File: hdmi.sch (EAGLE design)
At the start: 156 parts, among them IC1 FT2232HL, U0 6SLX45CSG324, U1 MT41J64M16, U2 TPD12S016RKTR, U3 TPD12S016RKTR, U4 TPD12S016RKTR, U5 MNR18, U6 MNR18, U8 20Mhz

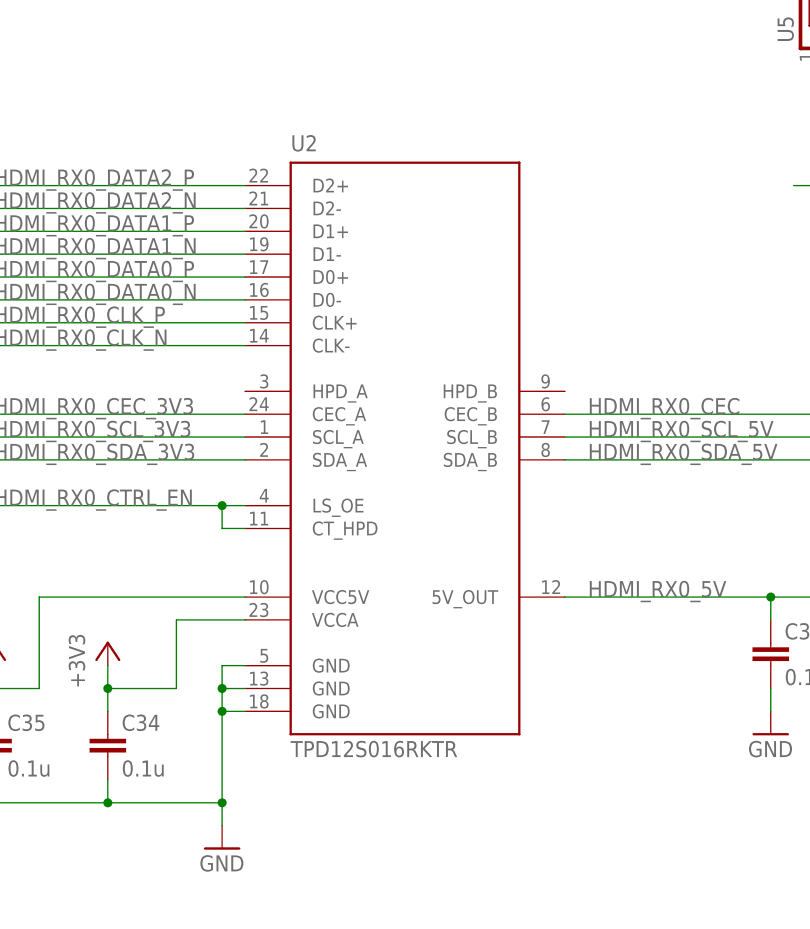
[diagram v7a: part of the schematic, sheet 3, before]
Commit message: Switched HDMI companion chip package, finished routing of the first HDMI group
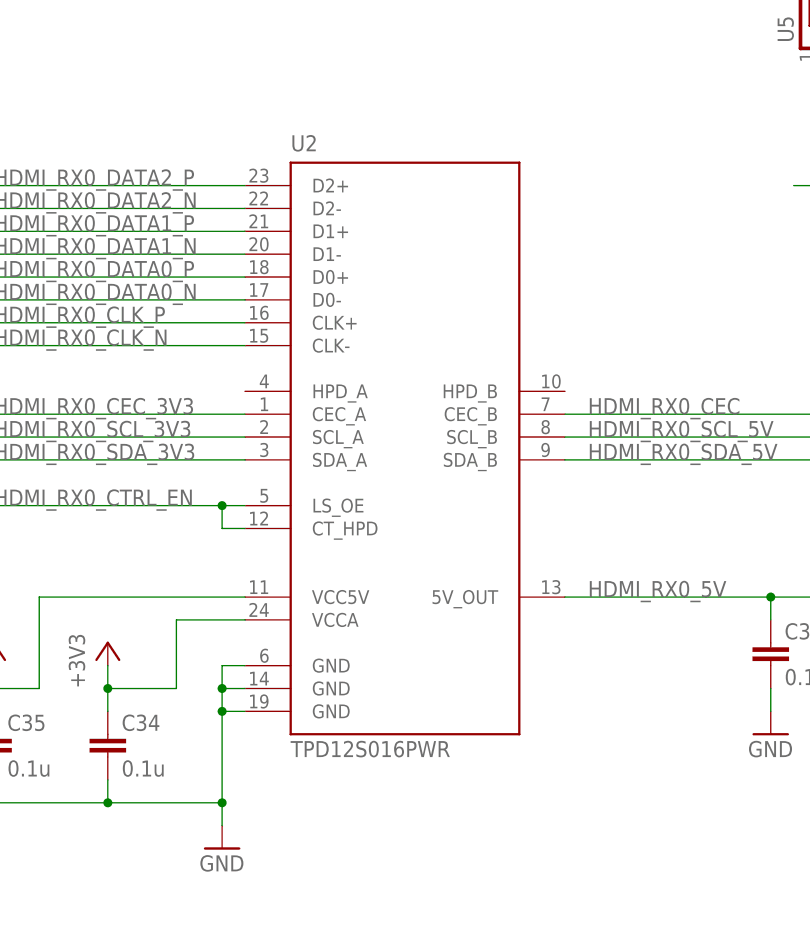
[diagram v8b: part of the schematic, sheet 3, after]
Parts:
- U2, U3, U4: value TPD12S016RKTR -> TPD12S016PWR; device prj-hdmi:TPD12S016RKTR -> prj-hdmi:TPD12S016PWR
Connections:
- net CENTER: now also SV3.1; no longer SV3.2
- net GND: now also SV3.2; no longer SV3.1
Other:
- moved on the sheet: SV3
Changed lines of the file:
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@@
 <part name="GND16" library="supply1" deviceset="GND" device=""/>
 <part name="C33" library="rcl" deviceset="C-EU" device="C0402" value="0.47u"/>
-<part name="U2" library="prj-hdmi" deviceset="TPD12S016" device="RKTR"/>
+<part name="U2" library="prj-hdmi" deviceset="TPD12S016" device="PWR" value="TPD12S016PWR"/>
 <part name="P+1" library="supply1" deviceset="+5V" device=""/>
 <part name="VCC4" library="supply1" deviceset="+3V3" device=""/>
@@
 <part name="CONN1" library="prj-hdmi" deviceset="HDMI_TYPE_A_RECEPTICAL" device=""/>
 <part name="GND17" library="supply1" deviceset="GND" device=""/>
-<part name="U3" library="prj-hdmi" deviceset="TPD12S016" device="RKTR"/>
+<part name="U3" library="prj-hdmi" deviceset="TPD12S016" device="PWR" value="TPD12S016PWR"/>
 <part name="P+2" library="supply1" deviceset="+5V" device=""/>
 <part name="VCC5" library="supply1" deviceset="+3V3" device=""/>
@@
 <part name="CONN2" library="prj-hdmi" deviceset="HDMI_TYPE_A_RECEPTICAL" device=""/>
 <part name="GND22" library="supply1" deviceset="GND" device=""/>
-<part name="U4" library="prj-hdmi" deviceset="TPD12S016" device="RKTR"/>
+<part name="U4" library="prj-hdmi" deviceset="TPD12S016" device="PWR" value="TPD12S016PWR"/>
 <part name="P+3" library="supply1" deviceset="+5V" device=""/>
 <part name="VCC6" library="supply1" deviceset="+3V3" device=""/>
@@
 <instance part="JP1" gate="1" x="157.48" y="154.94"/>
 <instance part="GND53" gate="1" x="154.94" y="137.16"/>
-<instance part="SV3" gate="G$1" x="137.16" y="144.78"/>
+<instance part="SV3" gate="G$1" x="137.16" y="142.24" rot="MR180"/>
 <instance part="GND47" gate="1" x="154.94" y="106.68"/>
 <instance part="C15" gate="G$1" x="172.72" y="139.7"/>
@@
 </segment>
 <segment>
-<pinref part="SV3" gate="G$1" pin="1"/>
+<pinref part="SV3" gate="G$1" pin="2"/>
 <pinref part="GND53" gate="1" pin="GND"/>
 <wire x1="144.78" y1="142.24" x2="154.94" y2="142.24" width="0.1524" layer="91"/>
@@
 <pinref part="JP1" gate="1" pin="1"/>
 <wire x1="154.94" y1="144.78" x2="154.94" y2="152.4" width="0.1524" layer="91"/>
-<pinref part="SV3" gate="G$1" pin="2"/>
+<pinref part="SV3" gate="G$1" pin="1"/>
 <wire x1="154.94" y1="144.78" x2="149.86" y2="144.78" width="0.1524" layer="91"/>
 <pinref part="DC_JACK" gate="G$1" pin="CENTER"/>
